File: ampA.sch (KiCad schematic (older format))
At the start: 13 parts, among them U2 screw_term, U3 screw_term, U4 screw_term, U7 TL084

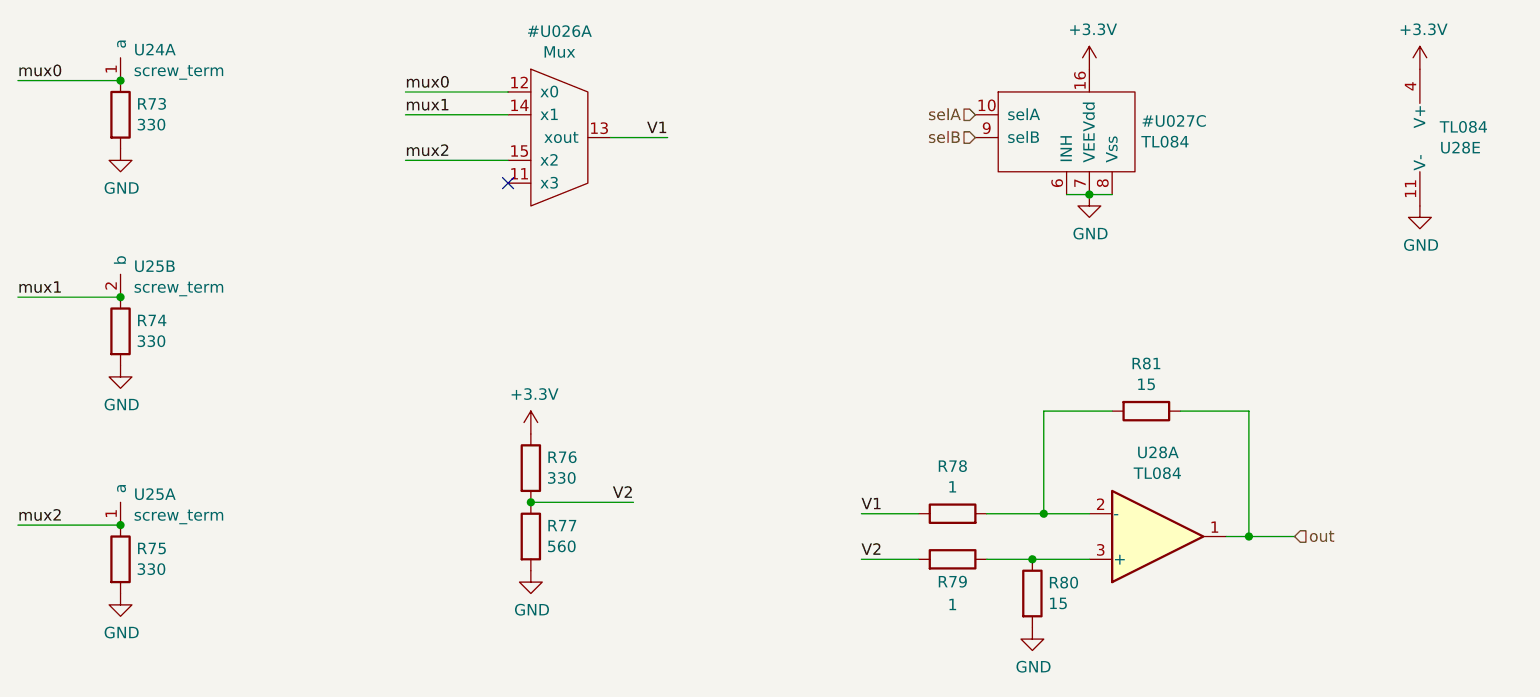
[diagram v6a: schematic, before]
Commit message: added all muxes to the board
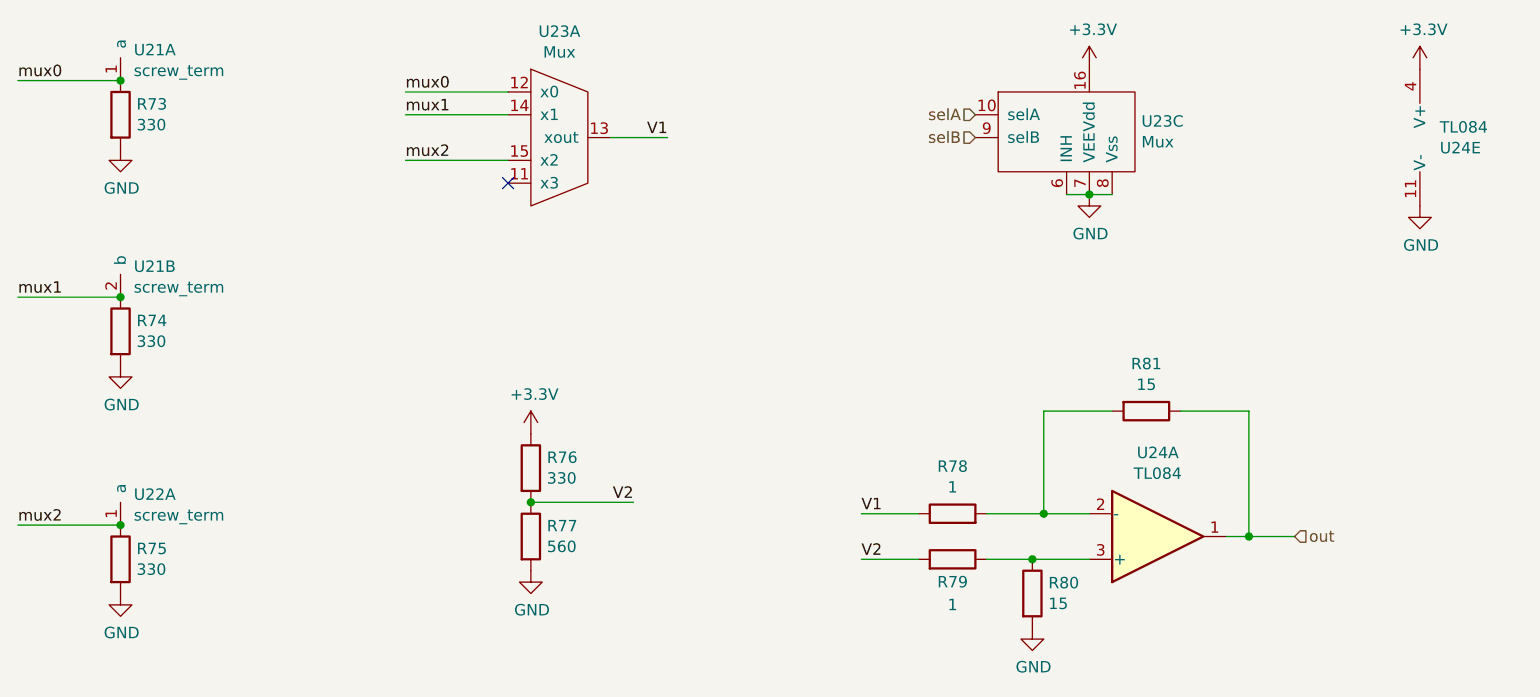
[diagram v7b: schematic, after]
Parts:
- added U5: Mux, Package_DIP:DIP-16_W7.62mm, symbol PNG_PCB_Parts:Mux
- renumbered U2 to U3, U7 to U6
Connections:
- net +3V3: now also U5.16 (Vdd)
- net GND: now also U5.6 (INH), U5.7 (VEE), U5.8 (Vss)
- net V1: now also U5.13 (xout)
- net mux0: now also U5.12 (x0)
- net mux1: now also U5.14 (x1)
- net mux2: now also U5.15 (x2)
- net selA: now also U5.10 (selA)
- net selB: now also U5.9 (selB)
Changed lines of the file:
@@
 P 6000 3800
 AR Path="/60132BC3/6013AE22/60198F31" Ref="U?"  Part="1"
-AR Path="/6017CC5E/60198F31" Ref="U7"  Part="1"
+AR Path="/6017CC5E/60198F31" Ref="U6"  Part="1"
 AR Path="/6017DA21/60198F31" Ref="U?"  Part="1"
 AR Path="/601927EB/60198F31" Ref="U?"  Part="1"
 AR Path="/6019C043/60198F31" Ref="U?"  Part="1"
-AR Path="/601B4C0E/60198F31" Ref="U12"  Part="1"
-AR Path="/601B73B7/60198F31" Ref="U28"  Part="1"
-F 0 "U28" H 6000 3433 50  0000 C CNN
+AR Path="/601B4C0E/60198F31" Ref="U15"  Part="1"
+AR Path="/601B73B7/60198F31" Ref="U24"  Part="1"
+F 0 "U24" H 6000 3433 50  0000 C CNN
 F 1 "TL084" H 6000 3524 50  0000 C CNN
 F 2 "Package_DIP:DIP-14_W7.62mm" H 5950 3900 50  0001 C CNN
@@
 $EndComp
 $Comp
-L PNG_PCB_Parts:Mux U?
-U 1 1 601709E6
-P 3350 2050
-AR Path="/60132BC3/6013AE22/601709E6" Ref="U?"  Part="1"
-AR Path="/6017CC5E/601709E6" Ref="#U05"  Part="1"
-AR Path="/6017DA21/601709E6" Ref="U?"  Part="1"
-AR Path="/601927EB/601709E6" Ref="U?"  Part="1"
-AR Path="/6019C043/601709E6" Ref="U?"  Part="1"
-AR Path="/601B4C0E/601709E6" Ref="#U016"  Part="1"
-AR Path="/601B73B7/601709E6" Ref="#U026"  Part="1"
-F 0 "#U026" H 3375 2515 50  0000 C CNN
-F 1 "Mux" H 3375 2424 50  0000 C CNN
-F 2 "Package_DIP:DIP-16_W7.62mm" H 3350 2050 50  0001 C CNN
-F 3 "" H 3350 2050 50  0001 C CNN
-	1    3350 2050
-	1    0    0    -1
-$EndComp
-$Comp
 L PNG_PCB_Parts:screw_term U?
 U 1 1 6016FA62
 P 1450 1800
 AR Path="/60132BC3/6013AE22/6016FA62" Ref="U?"  Part="1"
-AR Path="/6017CC5E/6016FA62" Ref="U2"  Part="1"
+AR Path="/6017CC5E/6016FA62" Ref="U3"  Part="1"
 AR Path="/6017DA21/6016FA62" Ref="U?"  Part="1"
 AR Path="/601927EB/6016FA62" Ref="U?"  Part="1"
 AR Path="/6019C043/6016FA62" Ref="U?"  Part="1"
-AR Path="/601B4C0E/6016FA62" Ref="U14"  Part="1"
-AR Path="/601B73B7/6016FA62" Ref="U24"  Part="1"
-F 0 "U24" H 1508 1934 50  0000 L CNN
+AR Path="/601B4C0E/6016FA62" Ref="U12"  Part="1"
+AR Path="/601B73B7/6016FA62" Ref="U21"  Part="1"
+F 0 "U21" H 1508 1934 50  0000 L CNN
 F 1 "screw_term" H 1508 1843 50  0000 L CNN
 F 2 "Connector_PinHeader_1.27mm:PinHeader_1x02_P1.27mm_Vertical" H 1450 1800 50  0001 C CNN
@@
 AR Path="/601927EB/60176F25" Ref="U?"  Part="2"
 AR Path="/6019C043/60176F25" Ref="U?"  Part="2"
-AR Path="/601B4C0E/60176F25" Ref="U15"  Part="2"
-AR Path="/601B73B7/60176F25" Ref="U25"  Part="2"
-F 0 "U25" H 1508 2884 50  0000 L CNN
+AR Path="/601B4C0E/60176F25" Ref="U12"  Part="2"
+AR Path="/601B73B7/60176F25" Ref="U21"  Part="2"
+F 0 "U21" H 1508 2884 50  0000 L CNN
 F 1 "screw_term" H 1508 2793 50  0000 L CNN
 F 2 "Connector_PinHeader_1.27mm:PinHeader_1x02_P1.27mm_Vertical" H 1450 2750 50  0001 C CNN
@@
 AR Path="/601927EB/6019D55C" Ref="U?"  Part="1"
 AR Path="/6019C043/6019D55C" Ref="U?"  Part="1"
-AR Path="/601B4C0E/6019D55C" Ref="U15"  Part="1"
-AR Path="/601B73B7/6019D55C" Ref="U25"  Part="1"
-F 0 "U25" H 1508 3884 50  0000 L CNN
+AR Path="/601B4C0E/6019D55C" Ref="U13"  Part="1"
+AR Path="/601B73B7/6019D55C" Ref="U22"  Part="1"
+F 0 "U22" H 1508 3884 50  0000 L CNN
 F 1 "screw_term" H 1508 3793 50  0000 L CNN
 F 2 "Connector_PinHeader_1.27mm:PinHeader_1x02_P1.27mm_Vertical" H 1450 3750 50  0001 C CNN
@@
 Text Label 2700 2150 0    50   ~ 0
 mux2
-$Comp
-L PNG_PCB_Parts:Mux #U06
-U 3 1 60186A46
-P 5700 2100
-AR Path="/6017CC5E/60186A46" Ref="#U06"  Part="3"
-AR Path="/601927EB/60186A46" Ref="U?"  Part="3"
-AR Path="/6019C043/60186A46" Ref="U?"  Part="3"
-AR Path="/601B4C0E/60186A46" Ref="#U017"  Part="3"
-AR Path="/601B73B7/60186A46" Ref="#U027"  Part="3"
-F 0 "#U027" H 5928 2221 50  0000 L CNN
-F 1 "TL084" H 5928 2130 50  0000 L CNN
-F 2 "" H 5700 2100 50  0001 C CNN
-F 3 "http://www.ti.com/lit/ds/symlink/tl081.pdf" H 5700 2100 50  0001 C CNN
-	3    5700 2100
-	1    0    0    -1
-$EndComp
 Wire Wire Line
 	5600 2300 5700 2300
@@
 P 7050 2050
 AR Path="/60132BC3/6013AE22/60194917" Ref="U?"  Part="1"
-AR Path="/6017CC5E/60194917" Ref="U7"  Part="5"
+AR Path="/6017CC5E/60194917" Ref="U6"  Part="5"
 AR Path="/6017DA21/60194917" Ref="U?"  Part="1"
 AR Path="/601927EB/60194917" Ref="U?"  Part="1"
 AR Path="/6019C043/60194917" Ref="U?"  Part="5"
-AR Path="/601B4C0E/60194917" Ref="U12"  Part="5"
-AR Path="/601B73B7/60194917" Ref="U28"  Part="5"
-F 0 "U28" H 6863 2004 50  0000 R CNN
+AR Path="/601B4C0E/60194917" Ref="U15"  Part="5"
+AR Path="/601B73B7/60194917" Ref="U24"  Part="5"
+F 0 "U24" H 6863 2004 50  0000 R CNN
 F 1 "TL084" H 6863 2095 50  0000 R CNN
 F 2 "Package_DIP:DIP-14_W7.62mm" H 7000 2150 50  0001 C CNN
@@
 	1    0    0    -1
 $EndComp
+$Comp
+L PNG_PCB_Parts:Mux U5
+U 1 1 6016DEDC
+P 3350 2050
+AR Path="/6017CC5E/6016DEDC" Ref="U5"  Part="1"
+AR Path="/601B4C0E/6016DEDC" Ref="U14"  Part="1"
+AR Path="/601B73B7/6016DEDC" Ref="U23"  Part="1"
+F 0 "U23" H 3375 2515 50  0000 C CNN
+F 1 "Mux" H 3375 2424 50  0000 C CNN
+F 2 "Package_DIP:DIP-16_W7.62mm" H 3350 2050 50  0001 C CNN
+F 3 "" H 3350 2050 50  0001 C CNN
+	1    3350 2050
+	1    0    0    -1
+$EndComp
+$Comp
+L PNG_PCB_Parts:Mux U5
+U 3 1 6016F806
+P 5700 2100
+AR Path="/6017CC5E/6016F806" Ref="U5"  Part="3"
+AR Path="/601B4C0E/6016F806" Ref="U14"  Part="3"
+AR Path="/601B73B7/6016F806" Ref="U23"  Part="3"
+F 0 "U23" H 5928 2221 50  0000 L CNN
+F 1 "Mux" H 5928 2130 50  0000 L CNN
+F 2 "Package_DIP:DIP-16_W7.62mm" H 5700 2100 50  0001 C CNN
+F 3 "" H 5700 2100 50  0001 C CNN
+	3    5700 2100
+	1    0    0    -1
+$EndComp

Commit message: changed to mcp6004 op amp
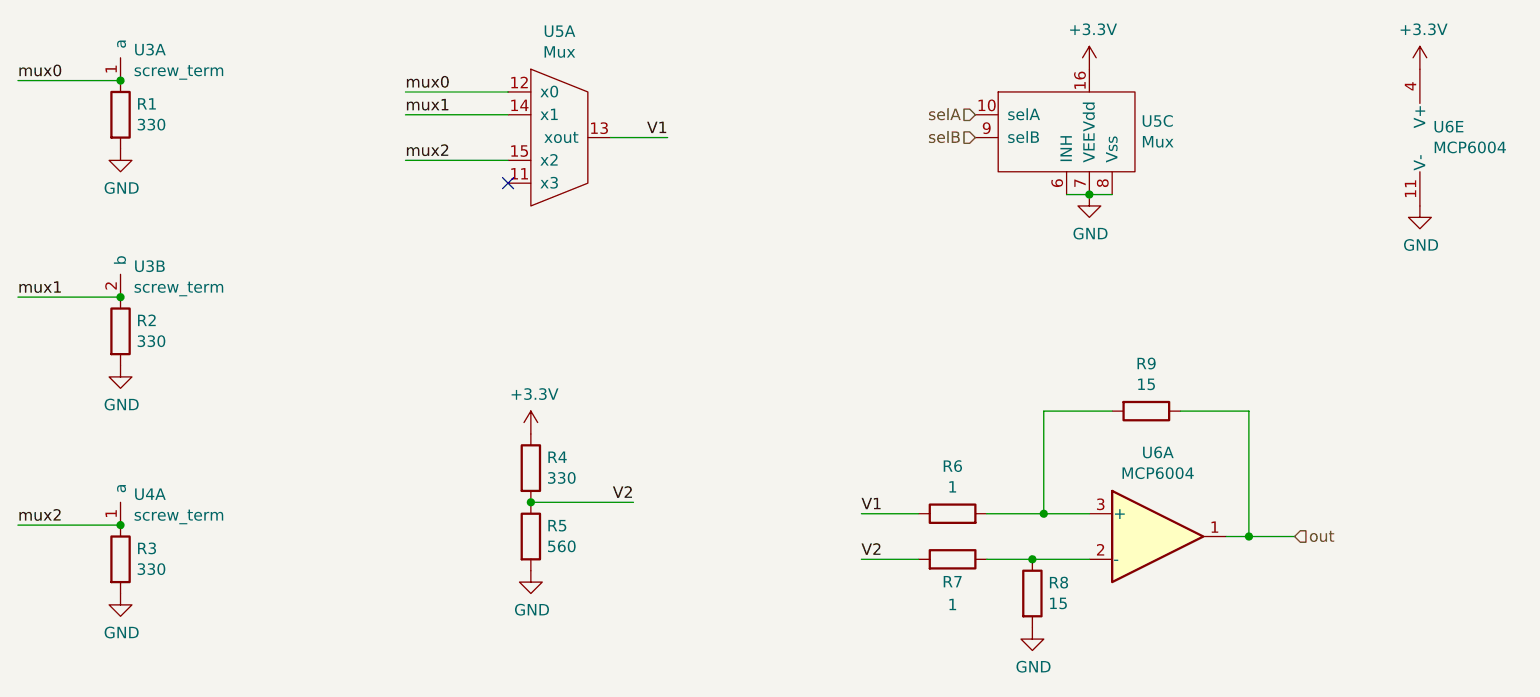
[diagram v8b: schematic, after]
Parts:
- removed U6: TL084, Package_DIP:DIP-14_W7.62mm, symbol Amplifier_Operational:TL084
- added U6: MCP6004, Package_DIP:DIP-14_W7.62mm, symbol Amplifier_Operational:MCP6004
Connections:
- net +3V3: now also U6.4 (V+)
- net GND: now also U6.11 (V-)
- net out: now also U6.1
- net at R6.2, R9.2: now also U6.3 (+)
- net at R7.1, R8.1: now also U6.2 (-)
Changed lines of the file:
@@
 $Descr A4 11693 8268
 encoding utf-8
-Sheet 10 11
+Sheet 2 11
 Title ""
 Date ""
@@
 AR Path="/601B4C0E/6013BAC9" Ref="#PWR038"  Part="1"
 AR Path="/601B73B7/6013BAC9" Ref="#PWR068"  Part="1"
-F 0 "#PWR068" H 1450 1850 50  0001 C CNN
+F 0 "#PWR08" H 1450 1850 50  0001 C CNN
 F 1 "GND" H 1455 1927 50  0000 C CNN
 F 2 "" H 1450 2100 50  0001 C CNN
@@
 	1    1450 2100
 	1    0    0    -1
-$EndComp
-$Comp
-L Amplifier_Operational:TL084 U?
-U 1 1 60198F31
-P 6000 3800
-AR Path="/60132BC3/6013AE22/60198F31" Ref="U?"  Part="1"
-AR Path="/6017CC5E/60198F31" Ref="U6"  Part="1"
-AR Path="/6017DA21/60198F31" Ref="U?"  Part="1"
-AR Path="/601927EB/60198F31" Ref="U?"  Part="1"
-AR Path="/6019C043/60198F31" Ref="U?"  Part="1"
-AR Path="/601B4C0E/60198F31" Ref="U15"  Part="1"
-AR Path="/601B73B7/60198F31" Ref="U24"  Part="1"
-F 0 "U24" H 6000 3433 50  0000 C CNN
-F 1 "TL084" H 6000 3524 50  0000 C CNN
-F 2 "Package_DIP:DIP-14_W7.62mm" H 5950 3900 50  0001 C CNN
-F 3 "http://www.ti.com/lit/ds/symlink/tl081.pdf" H 6050 4000 50  0001 C CNN
-	1    6000 3800
-	1    0    0    1
 $EndComp
 $Comp
@@
 AR Path="/601B4C0E/6019D565" Ref="R44"  Part="1"
 AR Path="/601B73B7/6019D565" Ref="R80"  Part="1"
-F 0 "R80" H 5520 4096 50  0000 L CNN
+F 0 "R8" H 5520 4096 50  0000 L CNN
 F 1 "15" H 5520 4005 50  0000 L CNN
 F 2 "Resistor_THT:R_Axial_DIN0204_L3.6mm_D1.6mm_P5.08mm_Horizontal" V 5380 4050 50  0001 C CNN
@@
 AR Path="/601B4C0E/60198F32" Ref="R45"  Part="1"
 AR Path="/601B73B7/60198F32" Ref="R81"  Part="1"
-F 0 "R81" V 5743 3250 50  0000 C CNN
+F 0 "R9" V 5743 3250 50  0000 C CNN
 F 1 "15" V 5834 3250 50  0000 C CNN
 F 2 "Resistor_THT:R_Axial_DIN0204_L3.6mm_D1.6mm_P5.08mm_Horizontal" V 5880 3250 50  0001 C CNN
@@
 AR Path="/601B4C0E/6017E431" Ref="R42"  Part="1"
 AR Path="/601B73B7/6017E431" Ref="R78"  Part="1"
-F 0 "R78" V 5307 3700 50  0000 C CNN
+F 0 "R6" V 5307 3700 50  0000 C CNN
 F 1 "1" V 5216 3700 50  0000 C CNN
 F 2 "Resistor_THT:R_Axial_DIN0204_L3.6mm_D1.6mm_P5.08mm_Horizontal" V 5030 3700 50  0001 C CNN
@@
 AR Path="/601B4C0E/6019D568" Ref="R43"  Part="1"
 AR Path="/601B73B7/6019D568" Ref="R79"  Part="1"
-F 0 "R79" V 5000 3900 50  0000 C CNN
+F 0 "R7" V 5000 3900 50  0000 C CNN
 F 1 "1" V 4900 3900 50  0000 C CNN
 F 2 "Resistor_THT:R_Axial_DIN0204_L3.6mm_D1.6mm_P5.08mm_Horizontal" V 5030 3900 50  0001 C CNN
@@
 AR Path="/601B4C0E/6019D55E" Ref="R40"  Part="1"
 AR Path="/601B73B7/6019D55E" Ref="R76"  Part="1"
-F 0 "R76" H 3320 3546 50  0000 L CNN
+F 0 "R4" H 3320 3546 50  0000 L CNN
 F 1 "330" H 3320 3455 50  0000 L CNN
 F 2 "Resistor_THT:R_Axial_DIN0204_L3.6mm_D1.6mm_P5.08mm_Horizontal" V 3180 3500 50  0001 C CNN
@@
 AR Path="/601B4C0E/6019D55F" Ref="R41"  Part="1"
 AR Path="/601B73B7/6019D55F" Ref="R77"  Part="1"
-F 0 "R77" H 3320 3846 50  0000 L CNN
+F 0 "R5" H 3320 3846 50  0000 L CNN
 F 1 "560" H 3320 3755 50  0000 L CNN
 F 2 "Resistor_THT:R_Axial_DIN0204_L3.6mm_D1.6mm_P5.08mm_Horizontal" V 3180 3800 50  0001 C CNN
@@
 AR Path="/601B4C0E/6019D560" Ref="#PWR041"  Part="1"
 AR Path="/601B73B7/6019D560" Ref="#PWR071"  Part="1"
-F 0 "#PWR071" H 3250 3200 50  0001 C CNN
+F 0 "#PWR011" H 3250 3200 50  0001 C CNN
 F 1 "+3.3V" H 3265 3523 50  0000 C CNN
 F 2 "" H 3250 3350 50  0001 C CNN
@@
 AR Path="/601B4C0E/60198F38" Ref="#PWR042"  Part="1"
 AR Path="/601B73B7/60198F38" Ref="#PWR072"  Part="1"
-F 0 "#PWR072" H 3250 3700 50  0001 C CNN
+F 0 "#PWR012" H 3250 3700 50  0001 C CNN
 F 1 "GND" H 3255 3777 50  0000 C CNN
 F 2 "" H 3250 3950 50  0001 C CNN
@@
 AR Path="/601B4C0E/6016B854" Ref="#PWR043"  Part="1"
 AR Path="/601B73B7/6016B854" Ref="#PWR073"  Part="1"
-F 0 "#PWR073" H 5450 3950 50  0001 C CNN
+F 0 "#PWR013" H 5450 3950 50  0001 C CNN
 F 1 "GND" H 5455 4027 50  0000 C CNN
 F 2 "" H 5450 4200 50  0001 C CNN
@@
 AR Path="/601B4C0E/6016D691" Ref="R37"  Part="1"
 AR Path="/601B73B7/6016D691" Ref="R73"  Part="1"
-F 0 "R73" H 1520 1996 50  0000 L CNN
+F 0 "R1" H 1520 1996 50  0000 L CNN
 F 1 "330" H 1520 1905 50  0000 L CNN
 F 2 "Resistor_THT:R_Axial_DIN0204_L3.6mm_D1.6mm_P5.08mm_Horizontal" V 1380 1950 50  0001 C CNN
@@
 AR Path="/601B4C0E/6016FA62" Ref="U12"  Part="1"
 AR Path="/601B73B7/6016FA62" Ref="U21"  Part="1"
-F 0 "U21" H 1508 1934 50  0000 L CNN
+F 0 "U3" H 1508 1934 50  0000 L CNN
 F 1 "screw_term" H 1508 1843 50  0000 L CNN
 F 2 "Connector_PinHeader_1.27mm:PinHeader_1x02_P1.27mm_Vertical" H 1450 1800 50  0001 C CNN
@@
 AR Path="/601B4C0E/6019D559" Ref="#PWR039"  Part="1"
 AR Path="/601B73B7/6019D559" Ref="#PWR069"  Part="1"
-F 0 "#PWR069" H 1450 2800 50  0001 C CNN
+F 0 "#PWR09" H 1450 2800 50  0001 C CNN
 F 1 "GND" H 1455 2877 50  0000 C CNN
 F 2 "" H 1450 3050 50  0001 C CNN
@@
 AR Path="/601B4C0E/6019D56A" Ref="R38"  Part="1"
 AR Path="/601B73B7/6019D56A" Ref="R74"  Part="1"
-F 0 "R74" H 1520 2946 50  0000 L CNN
+F 0 "R2" H 1520 2946 50  0000 L CNN
 F 1 "330" H 1520 2855 50  0000 L CNN
 F 2 "Resistor_THT:R_Axial_DIN0204_L3.6mm_D1.6mm_P5.08mm_Horizontal" V 1380 2900 50  0001 C CNN
@@
 AR Path="/601B4C0E/60176F25" Ref="U12"  Part="2"
 AR Path="/601B73B7/60176F25" Ref="U21"  Part="2"
-F 0 "U21" H 1508 2884 50  0000 L CNN
+F 0 "U3" H 1508 2884 50  0000 L CNN
 F 1 "screw_term" H 1508 2793 50  0000 L CNN
 F 2 "Connector_PinHeader_1.27mm:PinHeader_1x02_P1.27mm_Vertical" H 1450 2750 50  0001 C CNN
@@
 AR Path="/601B4C0E/6019D55B" Ref="#PWR040"  Part="1"
 AR Path="/601B73B7/6019D55B" Ref="#PWR070"  Part="1"
-F 0 "#PWR070" H 1450 3800 50  0001 C CNN
+F 0 "#PWR010" H 1450 3800 50  0001 C CNN
 F 1 "GND" H 1455 3877 50  0000 C CNN
 F 2 "" H 1450 4050 50  0001 C CNN
@@
 AR Path="/601B4C0E/6017E43F" Ref="R39"  Part="1"
 AR Path="/601B73B7/6017E43F" Ref="R75"  Part="1"
-F 0 "R75" H 1520 3946 50  0000 L CNN
+F 0 "R3" H 1520 3946 50  0000 L CNN
 F 1 "330" H 1520 3855 50  0000 L CNN
 F 2 "Resistor_THT:R_Axial_DIN0204_L3.6mm_D1.6mm_P5.08mm_Horizontal" V 1380 3900 50  0001 C CNN
@@
 AR Path="/601B4C0E/6019D55C" Ref="U13"  Part="1"
 AR Path="/601B73B7/6019D55C" Ref="U22"  Part="1"
-F 0 "U22" H 1508 3884 50  0000 L CNN
+F 0 "U4" H 1508 3884 50  0000 L CNN
 F 1 "screw_term" H 1508 3793 50  0000 L CNN
 F 2 "Connector_PinHeader_1.27mm:PinHeader_1x02_P1.27mm_Vertical" H 1450 3750 50  0001 C CNN
@@
 AR Path="/601B4C0E/601899DD" Ref="#PWR045"  Part="1"
 AR Path="/601B73B7/601899DD" Ref="#PWR075"  Part="1"
-F 0 "#PWR075" H 5700 2050 50  0001 C CNN
+F 0 "#PWR015" H 5700 2050 50  0001 C CNN
 F 1 "GND" H 5705 2127 50  0000 C CNN
 F 2 "" H 5700 2300 50  0001 C CNN
@@
 AR Path="/601B4C0E/60189E9E" Ref="#PWR044"  Part="1"
 AR Path="/601B73B7/60189E9E" Ref="#PWR074"  Part="1"
-F 0 "#PWR074" H 5700 1600 50  0001 C CNN
+F 0 "#PWR014" H 5700 1600 50  0001 C CNN
 F 1 "+3.3V" H 5715 1923 50  0000 C CNN
 F 2 "" H 5700 1750 50  0001 C CNN
@@
 Text HLabel 5200 2050 0    50   Input ~ 0
 selB
-$Comp
-L Amplifier_Operational:TL084 U?
-U 5 1 60194917
-P 7050 2050
-AR Path="/60132BC3/6013AE22/60194917" Ref="U?"  Part="1"
-AR Path="/6017CC5E/60194917" Ref="U6"  Part="5"
-AR Path="/6017DA21/60194917" Ref="U?"  Part="1"
-AR Path="/601927EB/60194917" Ref="U?"  Part="1"
-AR Path="/6019C043/60194917" Ref="U?"  Part="5"
-AR Path="/601B4C0E/60194917" Ref="U15"  Part="5"
-AR Path="/601B73B7/60194917" Ref="U24"  Part="5"
-F 0 "U24" H 6863 2004 50  0000 R CNN
-F 1 "TL084" H 6863 2095 50  0000 R CNN
-F 2 "Package_DIP:DIP-14_W7.62mm" H 7000 2150 50  0001 C CNN
-F 3 "http://www.ti.com/lit/ds/symlink/tl081.pdf" H 7100 2250 50  0001 C CNN
-	5    7050 2050
-	-1   0    0    -1
-$EndComp
 $Comp
 L power:GND #PWR?
@@
 AR Path="/601B4C0E/60195FF1" Ref="#PWR047"  Part="1"
 AR Path="/601B73B7/60195FF1" Ref="#PWR077"  Part="1"
-F 0 "#PWR077" H 7150 2100 50  0001 C CNN
+F 0 "#PWR017" H 7150 2100 50  0001 C CNN
 F 1 "GND" H 7155 2177 50  0000 C CNN
 F 2 "" H 7150 2350 50  0001 C CNN
@@
 AR Path="/601B4C0E/60198969" Ref="#PWR046"  Part="1"
 AR Path="/601B73B7/60198969" Ref="#PWR076"  Part="1"
-F 0 "#PWR076" H 7150 1600 50  0001 C CNN
+F 0 "#PWR016" H 7150 1600 50  0001 C CNN
 F 1 "+3.3V" H 7165 1923 50  0000 C CNN
 F 2 "" H 7150 1750 50  0001 C CNN
@@
 AR Path="/601B4C0E/6016DEDC" Ref="U14"  Part="1"
 AR Path="/601B73B7/6016DEDC" Ref="U23"  Part="1"
-F 0 "U23" H 3375 2515 50  0000 C CNN
+F 0 "U5" H 3375 2515 50  0000 C CNN
 F 1 "Mux" H 3375 2424 50  0000 C CNN
 F 2 "Package_DIP:DIP-16_W7.62mm" H 3350 2050 50  0001 C CNN
@@
 AR Path="/601B4C0E/6016F806" Ref="U14"  Part="3"
 AR Path="/601B73B7/6016F806" Ref="U23"  Part="3"
-F 0 "U23" H 5928 2221 50  0000 L CNN
+F 0 "U5" H 5928 2221 50  0000 L CNN
 F 1 "Mux" H 5928 2130 50  0000 L CNN
 F 2 "Package_DIP:DIP-16_W7.62mm" H 5700 2100 50  0001 C CNN
@@
 	1    0    0    -1
 $EndComp
+$Comp
+L Amplifier_Operational:MCP6004 U6
+U 1 1 60189002
+P 6000 3800
+AR Path="/6017CC5E/60189002" Ref="U6"  Part="1"
+AR Path="/601B4C0E/60189002" Ref="U15"  Part="1"
+AR Path="/601B73B7/60189002" Ref="U24"  Part="1"
+F 0 "U6" H 6000 4167 50  0000 C CNN
+F 1 "MCP6004" H 6000 4076 50  0000 C CNN
+F 2 "Package_DIP:DIP-14_W7.62mm" H 5950 3900 50  0001 C CNN
+F 3 "http://ww1.microchip.com/downloads/en/DeviceDoc/21733j.pdf" H 6050 4000 50  0001 C CNN
+	1    6000 3800
+	1    0    0    -1
+$EndComp
+$Comp
+L Amplifier_Operational:MCP6004 U6
+U 5 1 6018B5B8
+P 7250 2050
+AR Path="/6017CC5E/6018B5B8" Ref="U6"  Part="5"
+AR Path="/601B4C0E/6018B5B8" Ref="U15"  Part="5"
+AR Path="/601B73B7/6018B5B8" Ref="U24"  Part="5"
+F 0 "U6" H 7208 2096 50  0000 L CNN
+F 1 "MCP6004" H 7208 2005 50  0000 L CNN
+F 2 "Package_DIP:DIP-14_W7.62mm" H 7200 2150 50  0001 C CNN
+F 3 "http://ww1.microchip.com/downloads/en/DeviceDoc/21733j.pdf" H 7300 2250 50  0001 C CNN
+	5    7250 2050
+	1    0    0    -1
+$EndComp
